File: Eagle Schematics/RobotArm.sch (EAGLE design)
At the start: 87 parts, among them J1 5A/28V, SW1 5A/28V

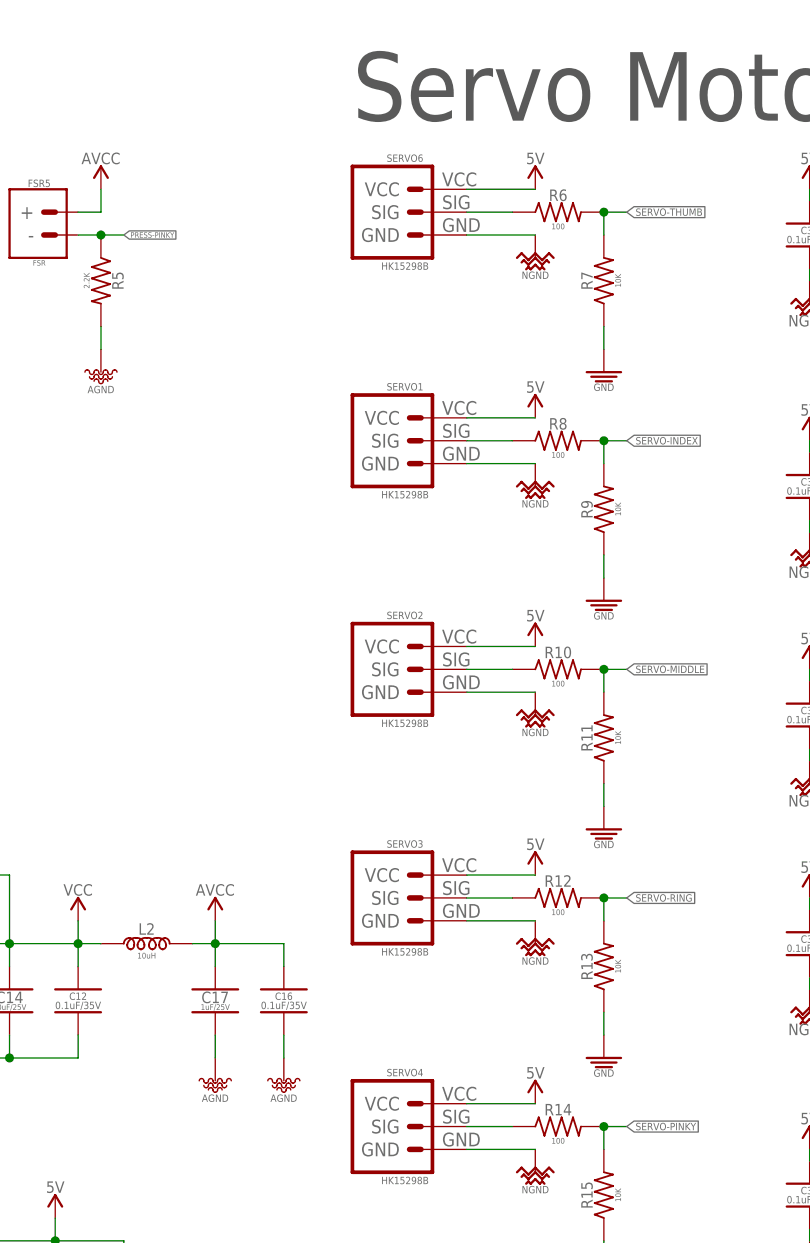
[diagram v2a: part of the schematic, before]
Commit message: I routed everything except for VCC. I am not sure how to proceed from here.
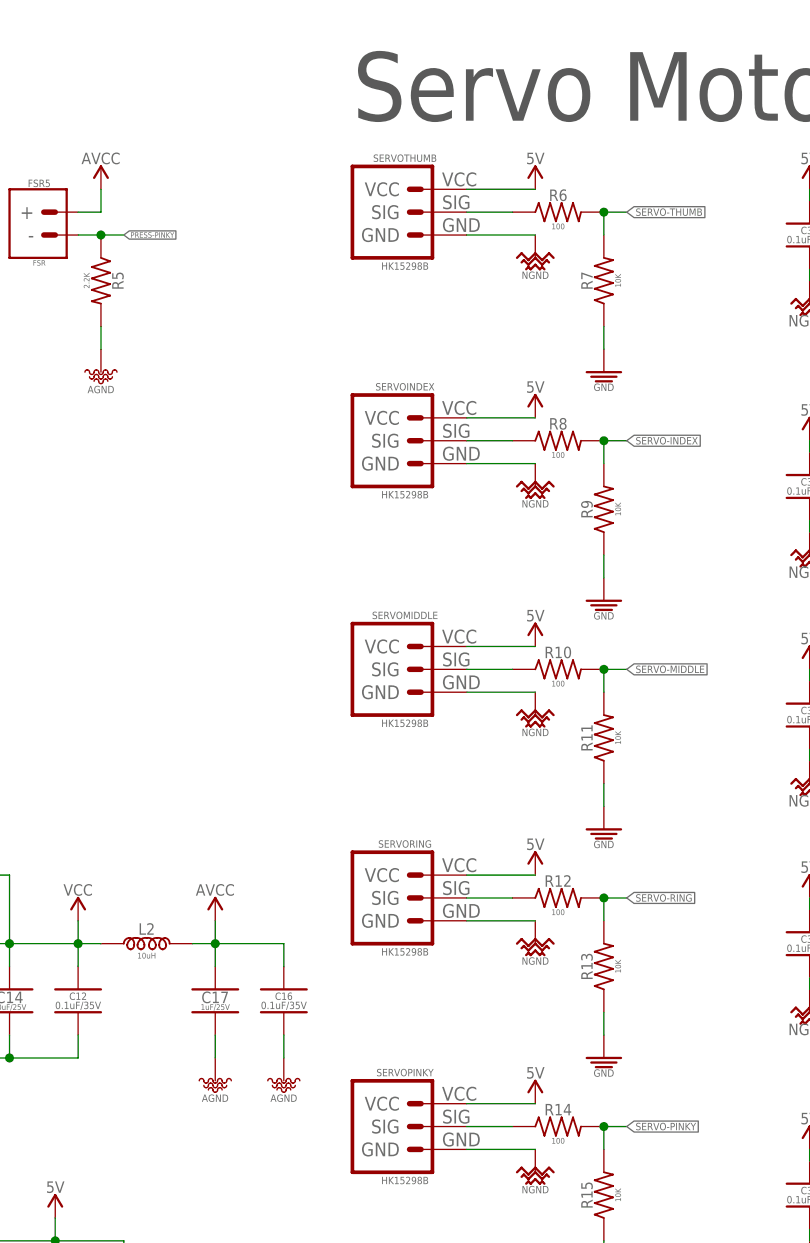
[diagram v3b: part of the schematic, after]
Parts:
- renumbered SERVO1 to SERVOINDEX, SERVO2 to SERVOMIDDLE, SERVO3 to SERVORING, SERVO4 to SERVOPINKY, SERVO6 to SERVOTHUMB
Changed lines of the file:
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@@
 <part name="SUPPLY10" library="PiB_power_symbols" deviceset="AGND" device=""/>
 <part name="R6" library="PiB_resistors" deviceset="100Ω" device="_SMD-0805_1/8W-5%" package3d_urn="urn:adsk.eagle:package:3034995/1" value="100"/>
-<part name="SERVO6" library="PiB_motors" deviceset="SERVO" device="_SERVO-PN" package3d_urn="urn:adsk.eagle:package:3035518/2" value="HK15298B"/>
+<part name="SERVOTHUMB" library="PiB_motors" deviceset="SERVO" device="_SERVO-PN" package3d_urn="urn:adsk.eagle:package:3035518/2" value="HK15298B"/>
 <part name="SUPPLY21" library="PiB_power_symbols" deviceset="5V" device=""/>
 <part name="SUPPLY22" library="PiB_power_symbols" deviceset="NGND" device=""/>
@@
 <part name="SUPPLY19" library="PiB_power_symbols" deviceset="GND" device=""/>
 <part name="R8" library="PiB_resistors" deviceset="100Ω" device="_SMD-0805_1/8W-5%" package3d_urn="urn:adsk.eagle:package:3034995/1" value="100"/>
-<part name="SERVO1" library="PiB_motors" deviceset="SERVO" device="_SERVO-PN" package3d_urn="urn:adsk.eagle:package:3035518/2" value="HK15298B"/>
+<part name="SERVOINDEX" library="PiB_motors" deviceset="SERVO" device="_SERVO-PN" package3d_urn="urn:adsk.eagle:package:3035518/2" value="HK15298B"/>
 <part name="SUPPLY11" library="PiB_power_symbols" deviceset="5V" device=""/>
 <part name="SUPPLY12" library="PiB_power_symbols" deviceset="NGND" device=""/>
@@
 <part name="SUPPLY13" library="PiB_power_symbols" deviceset="GND" device=""/>
 <part name="R10" library="PiB_resistors" deviceset="100Ω" device="_SMD-0805_1/8W-5%" package3d_urn="urn:adsk.eagle:package:3034995/1" value="100"/>
-<part name="SERVO2" library="PiB_motors" deviceset="SERVO" device="_SERVO-PN" package3d_urn="urn:adsk.eagle:package:3035518/2" value="HK15298B"/>
+<part name="SERVOMIDDLE" library="PiB_motors" deviceset="SERVO" device="_SERVO-PN" package3d_urn="urn:adsk.eagle:package:3035518/2" value="HK15298B"/>
 <part name="SUPPLY14" library="PiB_power_symbols" deviceset="5V" device=""/>
 <part name="SUPPLY15" library="PiB_power_symbols" deviceset="NGND" device=""/>
@@
 <part name="SUPPLY16" library="PiB_power_symbols" deviceset="GND" device=""/>
 <part name="R12" library="PiB_resistors" deviceset="100Ω" device="_SMD-0805_1/8W-5%" package3d_urn="urn:adsk.eagle:package:3034995/1" value="100"/>
-<part name="SERVO3" library="PiB_motors" deviceset="SERVO" device="_SERVO-PN" package3d_urn="urn:adsk.eagle:package:3035518/2" value="HK15298B"/>
+<part name="SERVORING" library="PiB_motors" deviceset="SERVO" device="_SERVO-PN" package3d_urn="urn:adsk.eagle:package:3035518/2" value="HK15298B"/>
 <part name="SUPPLY17" library="PiB_power_symbols" deviceset="5V" device=""/>
 <part name="SUPPLY18" library="PiB_power_symbols" deviceset="NGND" device=""/>
@@
 <part name="SUPPLY20" library="PiB_power_symbols" deviceset="GND" device=""/>
 <part name="R14" library="PiB_resistors" deviceset="100Ω" device="_SMD-0805_1/8W-5%" package3d_urn="urn:adsk.eagle:package:3034995/1" value="100"/>
-<part name="SERVO4" library="PiB_motors" deviceset="SERVO" device="_SERVO-PN" package3d_urn="urn:adsk.eagle:package:3035518/2" value="HK15298B"/>
+<part name="SERVOPINKY" library="PiB_motors" deviceset="SERVO" device="_SERVO-PN" package3d_urn="urn:adsk.eagle:package:3035518/2" value="HK15298B"/>
 <part name="SUPPLY23" library="PiB_power_symbols" deviceset="5V" device=""/>
 <part name="SUPPLY24" library="PiB_power_symbols" deviceset="NGND" device=""/>
@@
 <instance part="SUPPLY10" gate="G$1" x="25.4" y="40.64"/>
 <instance part="R6" gate="G$1" x="76.2" y="58.42"/>
-<instance part="SERVO6" gate="G$1" x="58.42" y="58.42"/>
+<instance part="SERVOTHUMB" gate="G$1" x="58.42" y="58.42"/>
 <instance part="SUPPLY21" gate="5V" x="73.66" y="60.96"/>
 <instance part="SUPPLY22" gate="G$1" x="73.66" y="53.34"/>
@@
 <instance part="SUPPLY19" gate="GND" x="81.28" y="40.64"/>
 <instance part="R8" gate="G$1" x="76.2" y="33.02"/>
-<instance part="SERVO1" gate="G$1" x="58.42" y="33.02"/>
+<instance part="SERVOINDEX" gate="G$1" x="58.42" y="33.02"/>
 <instance part="SUPPLY11" gate="5V" x="73.66" y="35.56"/>
 <instance part="SUPPLY12" gate="G$1" x="73.66" y="27.94"/>
@@
 <instance part="SUPPLY13" gate="GND" x="81.28" y="15.24"/>
 <instance part="R10" gate="G$1" x="76.2" y="7.62"/>
-<instance part="SERVO2" gate="G$1" x="58.42" y="7.62"/>
+<instance part="SERVOMIDDLE" gate="G$1" x="58.42" y="7.62"/>
 <instance part="SUPPLY14" gate="5V" x="73.66" y="10.16"/>
 <instance part="SUPPLY15" gate="G$1" x="73.66" y="2.54"/>
@@
 <instance part="SUPPLY16" gate="GND" x="81.28" y="-10.16"/>
 <instance part="R12" gate="G$1" x="76.2" y="-17.78"/>
-<instance part="SERVO3" gate="G$1" x="58.42" y="-17.78"/>
+<instance part="SERVORING" gate="G$1" x="58.42" y="-17.78"/>
 <instance part="SUPPLY17" gate="5V" x="73.66" y="-15.24"/>
 <instance part="SUPPLY18" gate="G$1" x="73.66" y="-22.86"/>
@@
 <instance part="SUPPLY20" gate="GND" x="81.28" y="-35.56"/>
 <instance part="R14" gate="G$1" x="76.2" y="-43.18"/>
-<instance part="SERVO4" gate="G$1" x="58.42" y="-43.18"/>
+<instance part="SERVOPINKY" gate="G$1" x="58.42" y="-43.18"/>
 <instance part="SUPPLY23" gate="5V" x="73.66" y="-40.64"/>
 <instance part="SUPPLY24" gate="G$1" x="73.66" y="-48.26"/>
@@
 <net name="N$1" class="0">
 <segment>
-<pinref part="SERVO6" gate="G$1" pin="SIG"/>
+<pinref part="SERVOTHUMB" gate="G$1" pin="SIG"/>
 <pinref part="R6" gate="G$1" pin="1"/>
 <wire x1="71.12" y1="58.42" x2="66.04" y2="58.42" width="0.1524" layer="91"/>
@@
 <net name="5V" class="0">
 <segment>
-<pinref part="SERVO6" gate="G$1" pin="VCC"/>
+<pinref part="SERVOTHUMB" gate="G$1" pin="VCC"/>
 <pinref part="SUPPLY21" gate="5V" pin="5V"/>
 <wire x1="66.04" y1="60.96" x2="73.66" y2="60.96" width="0.1524" layer="91"/>
 </segment>
 <segment>
-<pinref part="SERVO1" gate="G$1" pin="VCC"/>
+<pinref part="SERVOINDEX" gate="G$1" pin="VCC"/>
 <pinref part="SUPPLY11" gate="5V" pin="5V"/>
 <wire x1="66.04" y1="35.56" x2="73.66" y2="35.56" width="0.1524" layer="91"/>
 </segment>
 <segment>
-<pinref part="SERVO2" gate="G$1" pin="VCC"/>
+<pinref part="SERVOMIDDLE" gate="G$1" pin="VCC"/>
 <pinref part="SUPPLY14" gate="5V" pin="5V"/>
 <wire x1="66.04" y1="10.16" x2="73.66" y2="10.16" width="0.1524" layer="91"/>
 </segment>
 <segment>
-<pinref part="SERVO3" gate="G$1" pin="VCC"/>
+<pinref part="SERVORING" gate="G$1" pin="VCC"/>
 <pinref part="SUPPLY17" gate="5V" pin="5V"/>
 <wire x1="66.04" y1="-15.24" x2="73.66" y2="-15.24" width="0.1524" layer="91"/>
 </segment>
 <segment>
-<pinref part="SERVO4" gate="G$1" pin="VCC"/>
+<pinref part="SERVOPINKY" gate="G$1" pin="VCC"/>
 <pinref part="SUPPLY23" gate="5V" pin="5V"/>
 <wire x1="66.04" y1="-40.64" x2="73.66" y2="-40.64" width="0.1524" layer="91"/>
@@
 <segment>
 <pinref part="SUPPLY22" gate="G$1" pin="NGND"/>
-<pinref part="SERVO6" gate="G$1" pin="GND"/>
+<pinref part="SERVOTHUMB" gate="G$1" pin="GND"/>
 <wire x1="73.66" y1="55.88" x2="66.04" y2="55.88" width="0.1524" layer="91"/>
 </segment>
 <segment>
 <pinref part="SUPPLY12" gate="G$1" pin="NGND"/>
-<pinref part="SERVO1" gate="G$1" pin="GND"/>
+<pinref part="SERVOINDEX" gate="G$1" pin="GND"/>
 <wire x1="73.66" y1="30.48" x2="66.04" y2="30.48" width="0.1524" layer="91"/>
 </segment>
 <segment>
 <pinref part="SUPPLY15" gate="G$1" pin="NGND"/>
-<pinref part="SERVO2" gate="G$1" pin="GND"/>
+<pinref part="SERVOMIDDLE" gate="G$1" pin="GND"/>
 <wire x1="73.66" y1="5.08" x2="66.04" y2="5.08" width="0.1524" layer="91"/>
 </segment>
 <segment>
 <pinref part="SUPPLY18" gate="G$1" pin="NGND"/>
-<pinref part="SERVO3" gate="G$1" pin="GND"/>
+<pinref part="SERVORING" gate="G$1" pin="GND"/>
 <wire x1="73.66" y1="-20.32" x2="66.04" y2="-20.32" width="0.1524" layer="91"/>
 </segment>
 <segment>
 <pinref part="SUPPLY24" gate="G$1" pin="NGND"/>
-<pinref part="SERVO4" gate="G$1" pin="GND"/>
+<pinref part="SERVOPINKY" gate="G$1" pin="GND"/>
 <wire x1="73.66" y1="-45.72" x2="66.04" y2="-45.72" width="0.1524" layer="91"/>
 </segment>
@@
 <net name="N$3" class="0">
 <segment>
-<pinref part="SERVO1" gate="G$1" pin="SIG"/>
+<pinref part="SERVOINDEX" gate="G$1" pin="SIG"/>
 <pinref part="R8" gate="G$1" pin="1"/>
 <wire x1="71.12" y1="33.02" x2="66.04" y2="33.02" width="0.1524" layer="91"/>
@@
 <net name="N$4" class="0">
 <segment>
-<pinref part="SERVO2" gate="G$1" pin="SIG"/>
+<pinref part="SERVOMIDDLE" gate="G$1" pin="SIG"/>
 <pinref part="R10" gate="G$1" pin="1"/>
 <wire x1="71.12" y1="7.62" x2="66.04" y2="7.62" width="0.1524" layer="91"/>
@@
 <net name="N$5" class="0">
 <segment>
-<pinref part="SERVO3" gate="G$1" pin="SIG"/>
+<pinref part="SERVORING" gate="G$1" pin="SIG"/>
 <pinref part="R12" gate="G$1" pin="1"/>
 <wire x1="71.12" y1="-17.78" x2="66.04" y2="-17.78" width="0.1524" layer="91"/>
@@
 <net name="N$6" class="0">
 <segment>
-<pinref part="SERVO4" gate="G$1" pin="SIG"/>
+<pinref part="SERVOPINKY" gate="G$1" pin="SIG"/>
 <pinref part="R14" gate="G$1" pin="1"/>
 <wire x1="71.12" y1="-43.18" x2="66.04" y2="-43.18" width="0.1524" layer="91"/>

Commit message: last update
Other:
- note removed: "Analog pins reading directly from sensors"
- moved on the sheet: ANT1, AVR_ISP1, BALUN1, C1, C10, C11, C12, C13, C14, C15, C16, C17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

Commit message: Massaged around some stuff.
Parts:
- removed D2: (no value), PiB_discrete_semiconductors:DIODE_GENERAL-PURPOSE_SMD_GP_1A-50V
- C23, C24: value 470uF/50V -> 1000uF/16V; device PiB_capacitors:470UF-POLARIZED -> PiB_capacitors:1000UF-POLARIZED_PTH_16V-20%
- C32, C33, C34, C35, C36: value 0.1uF/50V -> 10uF/25V; device PiB_capacitors:0.1UF_SMD-0402_50V-10% -> PiB_capacitors:10UF_CER_SMD-0805_25V-10%
- D1, D3: value (none) -> 1A/50V
- FSR1, FSR2, FSR3, FSR4, FSR5: value FSR -> 10K; device PiB:FSR_FORCE-SENSATIVE-RESISTOR_PRESS-SENSOR -> PiB_sensors:FORCE-SENSITIVE-RESISTOR_SENSOR_FSR-5MM_0530470210_VERT-MALE_PITCH-1.25MM
- R20, R21: value 1K -> 10K; device PiB_resistors:1KΩ_SMD-0805_1/8W-5% -> PiB_resistors:10KΩ_SMD-0805_1/8W-5%
- SERVOINDEX, SERVOMIDDLE, SERVOPINKY, SERVORING, SERVOTHUMB: value HK15298B -> MG90S; device PiB_motors:SERVO_SERVO-PN -> PiB:SERVO_MG90S_1X03_VERT_MALE
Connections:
- removed net 3.3V: AVR_ISP1.VCC
- removed net N$21: MCU1.(PCINT8/RXD0/D0)PE0
- removed net N$22: MCU1.(TXD0/D1)PE1
- net AGND: now also R1.2, R2.2, R3.2, R4.2, R5.2
- net GND: no longer R1.2, R2.2, R3.2, R4.2, R5.2
- net RX0: now also MCU1.(PCINT8/RXD0/D0)PE0
- net TX0: now also MCU1.(TXD0/D1)PE1
- net VBAT: no longer D2.K
- net VCC: no longer D2.A, FTDI1.VCC
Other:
- moved on the sheet: SW1

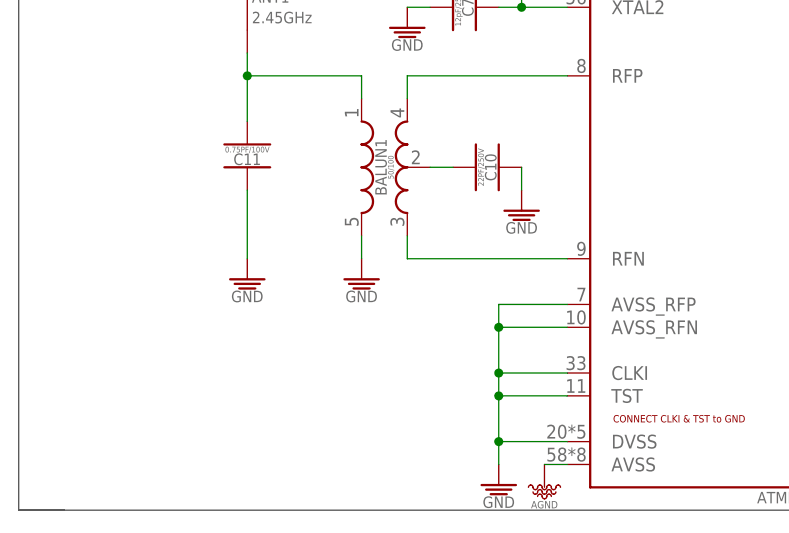
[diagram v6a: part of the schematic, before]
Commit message: Create antenna CKTry.
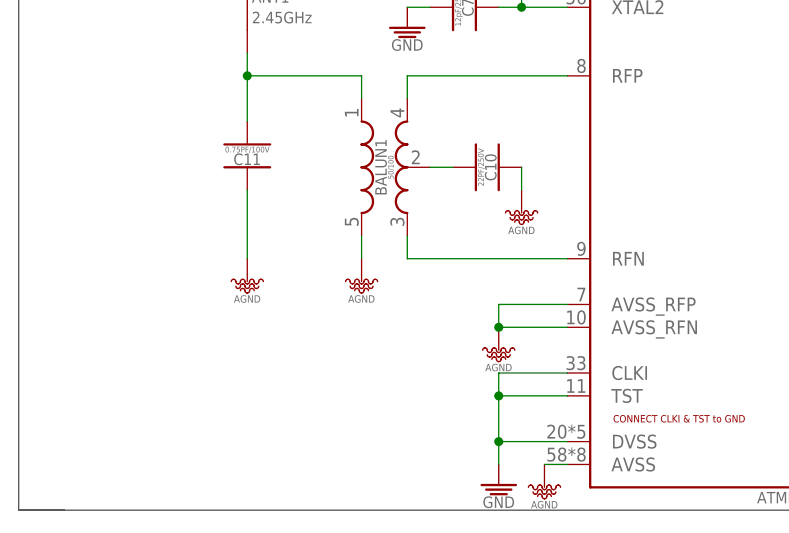
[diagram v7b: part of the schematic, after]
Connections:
- net AGND: now also BALUN1.GND@5, C10.1, C11.1, MCU1.AVSS_RFN, MCU1.AVSS_RFP
- net GND: no longer BALUN1.GND@5, C10.1, C11.1, MCU1.AVSS_RFN, MCU1.AVSS_RFP
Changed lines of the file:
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@@
 <drawing>
 <settings>
-<setting alwaysvectorfont="no"/>
+<setting alwaysvectorfont="yes"/>
 <setting verticaltext="up"/>
 </settings>
@@
 <part name="C10" library="PiB_capacitors" deviceset="22PF" device="_SMD-805_250V-5%" value="22PF/250V"/>
 <part name="C11" library="PiB_capacitors" deviceset="0.75PF" device="_SMD-805_100V-33%" value="0.75PF/100V"/>
-<part name="SUPPLY43" library="PiB_power_symbols" deviceset="GND" device=""/>
-<part name="SUPPLY44" library="PiB_power_symbols" deviceset="GND" device=""/>
 <part name="BALUN1" library="PiB_radio_frequency" deviceset="BALUN" device="_SMD-0805_UNBAL/BAL-50/100" package3d_urn="urn:adsk.eagle:package:2933573/1" value="50/100"/>
-<part name="SUPPLY45" library="PiB_power_symbols" deviceset="GND" device=""/>
 <part name="ANT1" library="PiB_radio_frequency" deviceset="ANTENNA" device="_SMD_CHP-2.45GHZ-0.5DBI-3W" package3d_urn="urn:adsk.eagle:package:2933495/1" value="2.45GHz"/>
 <part name="SUPPLY46" library="PiB_power_symbols" deviceset="GND" device=""/>
@@
 <part name="SUPPLY8" library="PiB_power_symbols" deviceset="AGND" device=""/>
 <part name="SUPPLY10" library="PiB_power_symbols" deviceset="AGND" device=""/>
+<part name="SUPPLY26" library="PiB_power_symbols" deviceset="AGND" device=""/>
+<part name="SUPPLY29" library="PiB_power_symbols" deviceset="AGND" device=""/>
+<part name="SUPPLY43" library="PiB_power_symbols" deviceset="AGND" device=""/>
+<part name="SUPPLY44" library="PiB_power_symbols" deviceset="AGND" device=""/>
 </parts>
 <sheets>
@@
 <instance part="C10" gate="G$1" x="-254" y="-15.24" rot="R270"/>
 <instance part="C11" gate="G$1" x="-281.94" y="-15.24" rot="R180"/>
-<instance part="SUPPLY43" gate="GND" x="-281.94" y="-27.94"/>
-<instance part="SUPPLY44" gate="GND" x="-269.24" y="-27.94"/>
 <instance part="BALUN1" gate="G$1" x="-266.7" y="-15.24"/>
-<instance part="SUPPLY45" gate="GND" x="-251.46" y="-20.32"/>
 <instance part="ANT1" gate="G$1" x="-281.94" y="2.54"/>
 <instance part="SUPPLY46" gate="GND" x="-254" y="-50.8"/>
@@
 <instance part="SUPPLY8" gate="G$1" x="2.54" y="40.64"/>
 <instance part="SUPPLY10" gate="G$1" x="22.86" y="40.64"/>
+<instance part="SUPPLY26" gate="G$1" x="-269.24" y="-27.94"/>
+<instance part="SUPPLY29" gate="G$1" x="-281.94" y="-27.94"/>
+<instance part="SUPPLY43" gate="G$1" x="-251.46" y="-20.32"/>
+<instance part="SUPPLY44" gate="G$1" x="-254" y="-35.56"/>
 </instances>
 <busses>
@@
 </segment>
 <segment>
-<pinref part="SUPPLY45" gate="GND" pin="GND"/>
-<pinref part="C10" gate="G$1" pin="1"/>
-<wire x1="-251.46" y1="-17.78" x2="-251.46" y2="-15.24" width="0.1524" layer="91"/>
-</segment>
-<segment>
-<pinref part="BALUN1" gate="G$1" pin="GND@5"/>
-<pinref part="SUPPLY44" gate="GND" pin="GND"/>
-<wire x1="-269.24" y1="-22.86" x2="-269.24" y2="-25.4" width="0.1524" layer="91"/>
-</segment>
-<segment>
-<pinref part="C11" gate="G$1" pin="1"/>
-<pinref part="SUPPLY43" gate="GND" pin="GND"/>
-<wire x1="-281.94" y1="-17.78" x2="-281.94" y2="-25.4" width="0.1524" layer="91"/>
-</segment>
-<segment>
-<pinref part="MCU1" gate="G$1" pin="AVSS_RFP"/>
-<wire x1="-246.38" y1="-30.48" x2="-254" y2="-30.48" width="0.1524" layer="91"/>
-<wire x1="-254" y1="-30.48" x2="-254" y2="-33.02" width="0.1524" layer="91"/>
-<pinref part="MCU1" gate="G$1" pin="AVSS_RFN"/>
-<wire x1="-254" y1="-33.02" x2="-254" y2="-38.1" width="0.1524" layer="91"/>
-<wire x1="-246.38" y1="-33.02" x2="-254" y2="-33.02" width="0.1524" layer="91"/>
-<junction x="-254" y="-33.02"/>
 <pinref part="MCU1" gate="G$1" pin="TST"/>
 <wire x1="-246.38" y1="-40.64" x2="-254" y2="-40.64" width="0.1524" layer="91"/>
@@
 <wire x1="-254" y1="-45.72" x2="-254" y2="-48.26" width="0.1524" layer="91"/>
 <wire x1="-246.38" y1="-38.1" x2="-254" y2="-38.1" width="0.1524" layer="91"/>
-<junction x="-254" y="-38.1"/>
 <pinref part="SUPPLY46" gate="GND" pin="GND"/>
 <pinref part="MCU1" gate="G$1" pin="DVSS"/>
@@
 <pinref part="SUPPLY10" gate="G$1" pin="AGND"/>
 </segment>
-</net>
+<segment>
+<pinref part="BALUN1" gate="G$1" pin="GND@5"/>
+<wire x1="-269.24" y1="-22.86" x2="-269.24" y2="-25.4" width="0.1524" layer="91"/>
+<pinref part="SUPPLY26" gate="G$1" pin="AGND"/>
+</segment>
+<segment>
+<pinref part="C11" gate="G$1" pin="1"/>
+<wire x1="-281.94" y1="-17.78" x2="-281.94" y2="-25.4" width="0.1524" layer="91"/>
+<pinref part="SUPPLY29" gate="G$1" pin="AGND"/>
+</segment>
+<segment>
+<pinref part="C10" gate="G$1" pin="1"/>
+<wire x1="-251.46" y1="-17.78" x2="-251.46" y2="-15.24" width="0.1524" layer="91"/>
+<pinref part="SUPPLY43" gate="G$1" pin="AGND"/>
+</segment>
+<segment>
+<pinref part="MCU1" gate="G$1" pin="AVSS_RFN"/>
+<wire x1="-246.38" y1="-33.02" x2="-254" y2="-33.02" width="0.1524" layer="91"/>
+<wire x1="-254" y1="-30.48" x2="-254" y2="-33.02" width="0.1524" layer="91"/>
+<pinref part="MCU1" gate="G$1" pin="AVSS_RFP"/>
+<wire x1="-246.38" y1="-30.48" x2="-254" y2="-30.48" width="0.1524" layer="91"/>
+<pinref part="SUPPLY44" gate="G$1" pin="AGND"/>
+<junction x="-254" y="-33.02"/>
+</segment>
+</net>
